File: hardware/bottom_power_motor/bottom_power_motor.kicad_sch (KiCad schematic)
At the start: 102 parts, among them J1 Power/Motor 6p, J2 J_STK_A, J3 J_STK_B, Q1 P-FET 40V 30A, U1 L78L12, U2 TPS54360, U2_CB 100n, U2_CO 47u, U2_CZ 3n3, U2_D 60V 3A, U2_L 10u, U2_RC 10k, U2_RH 53k6, U2_RL 10k2, U2_RT_R 100k, U3 TLV62569, U4 TPS54360, U4_CB 100n, U4_CO 22u, U4_CZ 3n3, U4_D 60V 3A, U4_L 33u, U4_RC 10k, U4_RH 68k1, U4_RL 10k0, U4_RT_R 100k

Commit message: Reed-Kontakte, Haubenkontakt, Klinkenbuchse, ToF statt Radar
Funktional neu
--------------
- Zwei Reed-Eingaenge fuer Fensterkontakte auf den einzigen noch freien
  Expanderpins P6/P7. 10k Pullup, 1k Serie, 100n und TVS je Kanal; bei
  geschlossenem Kontakt liegen 0,3 V am PCF8574, sicher unter VIL.
- Meldekontakt zur Dunstabzugshaube ueber PhotoMOS AQY282GS statt Relais:
  potentialfrei, 60 V / 0,8 A, kein Spulenstrom, keine Bauhoehe im 9-mm-
  Stapelspalt. NUR SELV - bei 230 V gehoert das Schaltglied nicht in die Dose.
- Weihnachtsstern jetzt gesteckt: Klinkenbuchse im oberen Steg der
  Frontplatte, PTC 0,2 A direkt an der Buchse gegen den Kurzschluss beim
  Stecken, Bulk vor die Sicherung gelegt.
- Radar durch VL53L1X (ToF) ersetzt. Hinter dieser Frontplatte hat kein
  20-mm-Radarmodul freie Sicht; der ToF passt als 4,9 x 2,5 mm grosser Chip
  in den Steg. Er misst Entfernung statt Empfindlichkeit - Schwelle exakt
  1 m - und deckt in der Fensterlaibung zugleich den Durchstieg ab.
  Netze umbenannt: RADAR_INT -> PRESENCE_INT, UART_RADAR_* -> UART_AUX_*.
  J7 bleibt unbestueckt als Reserve, damit das Stackpinout unberuehrt bleibt.

Frontplatte
-----------
Oberer Steg 9 -> 17 mm, damit Klinkenbuchse und ToF-Fenster nebeneinander
passen; Sicheln dadurch ~70 -> ~45 Grad, Stoesselwinkel 18 -> 12 Grad.
ToF-Kanal konisch (4,5 vorn, 3,0 hinten) fuer den Sichtkegel. Kabelausgang
Ø4,5 entfaellt. Selbsttests bestanden, STEP/STL neu erzeugt.

KiCad 10
--------
Die Generatoren liefen nur gegen KiCad-9-Bibliotheken. Migriert:
- Symbol- und Footprintpfad werden gefunden (Linux, macOS, Umgebungsvariable)
- PCF8574 -> PCF8574T (pinkompatibel, als Alias)
- Q_NMOS_GDS/Q_PMOS_GSD/Q_NPN_BCE liegen jetzt als hardware/lib/
  SwitchStack.kicad_sym im Projekt. KiCad 10 nummeriert die Stockvarianten
  mit G/D/S bzw. B/C/E - ein Alias haette die Anschluesse still vertauscht.
- USB-C-Schirm heisst SH statt S1, Zonen-API SetDoNotAllowZoneFills,
  DRC laeuft ueber kicad-cli statt WriteDRCRepo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
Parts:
- Q1: symbol Device:Q_PMOS_GSD -> SwitchStack:Q_PMOS_GSD
- Q_M1A_H, Q_M1A_L, Q_M1B_H, Q_M1B_L, Q_M2A_H, Q_M2A_L, Q_M2B_H, Q_M2B_L: symbol Device:Q_NMOS_GDS -> SwitchStack:Q_NMOS_GDS
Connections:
- net RADAR_INT renamed PRESENCE_INT
- net UART_RADAR_RX renamed UART_AUX_RX
- net UART_RADAR_TX renamed UART_AUX_TX
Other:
- moved on the sheet: R_M1_SH, R_M2_SH

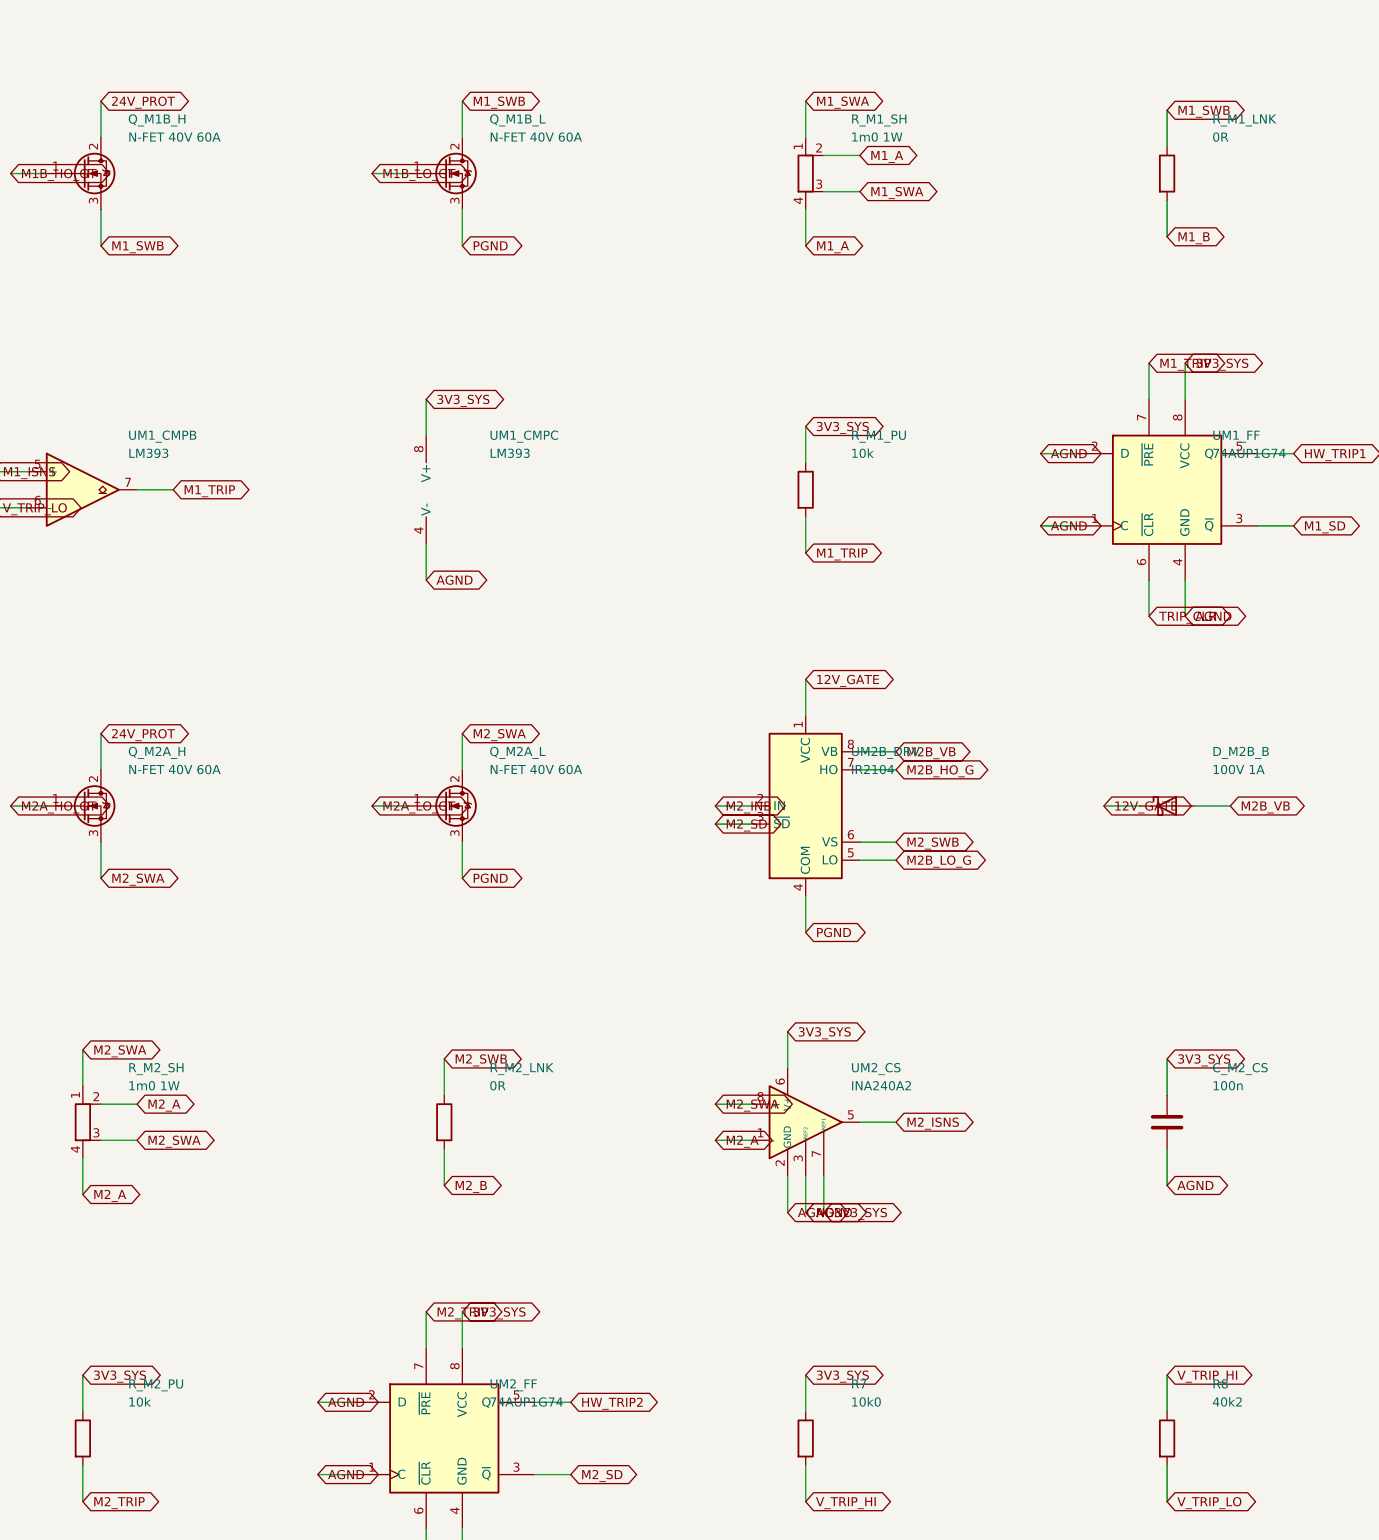
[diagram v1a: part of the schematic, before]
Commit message: Blockierstrom gemessen: 1,6 A statt 25 A - Auslegung neu gerechnet
Am 17.08.2026 mit blockiertem Abtrieb gemessen: 1,6 A bei 24 V, Netzteil mit
5 A Reserve, also keine Strombegrenzung. Daraus R_Anker = 15 Ohm. Die Messung
vom Vortag (0,116 A bei 2 V, 17,2 Ohm) bestaetigt das aus einem zwoelffach
anderen Betriebspunkt - die Zwischenbewertung "unbrauchbar" war falsch und ist
zurueckgenommen. Aufgeloest ist damit auch der Widerspruch zum Typenschild:
24 V an 15 Ohm ergeben maximal 38 W, die 100 W sind die Netzteilempfehlung der
Anlage, nicht die Aufnahme eines Motors.

GEAENDERTE WERTE - kein Layout betroffen:

  Shunt R_M1_SH/R_M2_SH   1 mOhm -> 5 mOhm    (gleicher Footprint)
  Trip-Teiler R8          40k2   -> 30k9      (+/-22 A -> +/-4,0 A)
  Sicherung F1            15 A   -> 6,3 A traege
  Firmware-Skalierung     20 A/V -> 4 A/V

Der Shunt wird groesser, nicht kleiner: Er bestimmt nicht die Belastbarkeit,
sondern die Aufloesung. Am 1-mOhm-Shunt lagen zwischen Fahrt und Anschlag nur
30-65 mV, in der Groessenordnung des ADC-Rauschens. Mit 5 mOhm sind es
150-325 mV bei 0,25 V/A und +/-6,6 A Messbereich; die Verlustleistung betraegt
bei 2 A ganze 20 mW.

Die Trip-Schwelle muss UEBER dem Blockierstrom liegen, weil der Anschlag ohne
Endschalter ein normaler Betriebszustand ist - der Laden faehrt bei jeder Fahrt
kurz dagegen. 4,0 A gibt Faktor 2,5 Reserve, ein echter Kurzschluss liegt
Groessenordnungen darueber.

FEHLER IN DER FIRMWARE MITGEFUNDEN: Der Nullpunkt des INA240 wurde nirgends
abgezogen. Der Sensor haette im Stillstand 6,6 A gemeldet statt 0 A. Jetzt
Betragsbildung um einen einstellbaren Nullpunkt (Vorgabe 1,65 V), damit auch
die Richtungsumkehr am Inline-Shunt kein Vorzeichen mehr erzeugt.

WAS DIE MESSUNG ERLEDIGT: Punkt 1 (Blockierstrom), Punkt 2 (Steckverbinder -
Micro-Fit 3.0 reicht, Mini-Fit Jr. nicht noetig) und die Verschaerfung von
Punkt 3. Der Summenstrom faellt von 9 A auf 3,9 A im unguenstigsten Fall.
Ein Anlaufstrom ueber dem Blockierstrom existier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
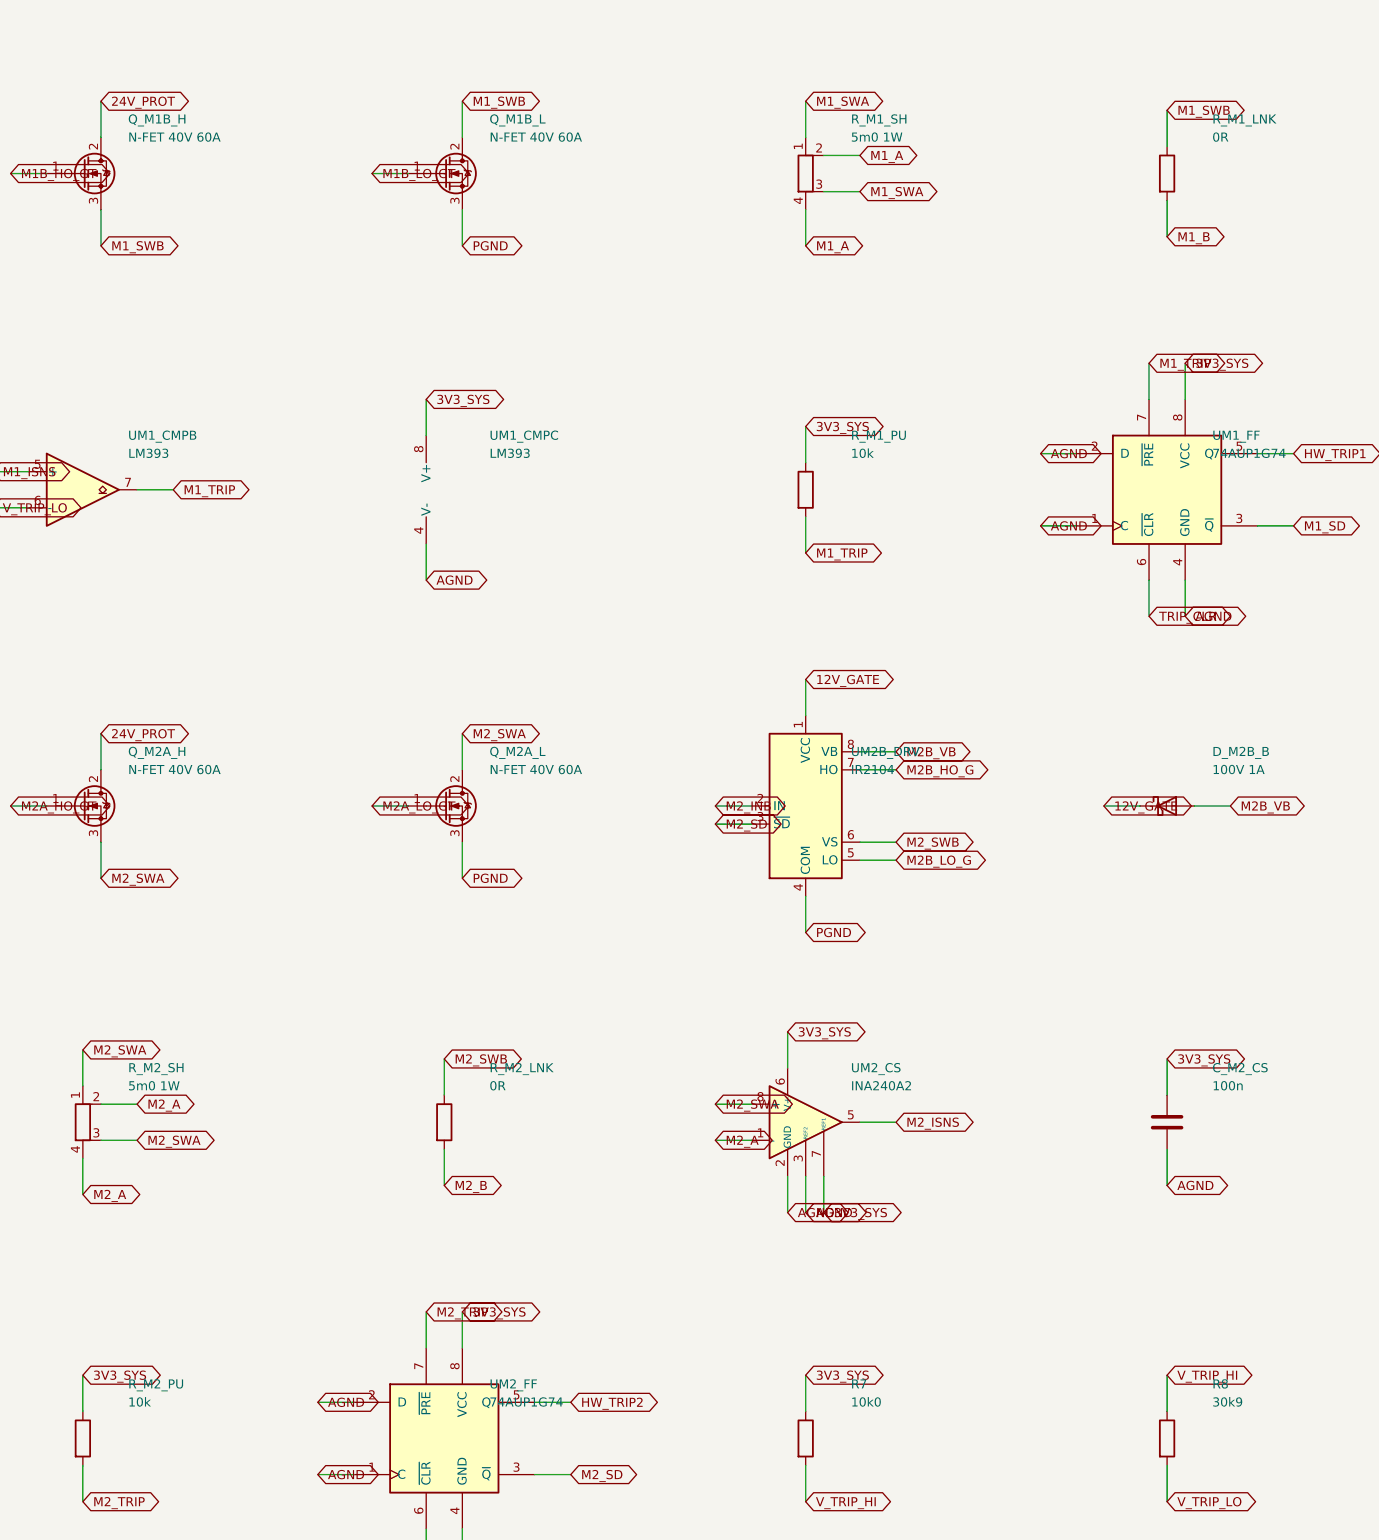
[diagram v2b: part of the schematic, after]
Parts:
- R7, R9: MPN Trip-Schwelle - messabhaengig -> Trip-Schwelle 4,0 A
- R8: value 40k2 -> 30k9; MPN Trip-Schwelle - messabhaengig -> Trip-Schwelle 4,0 A
- R_M1_SH, R_M2_SH: value 1m0 1W -> 5m0 1W
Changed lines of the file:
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@@
     (property "Reference" "R_M1_SH" (at 387.3500 284.4800 0)
       (effects (font (size 1.27 1.27)) (justify left)))
-    (property "Value" "1m0 1W" (at 387.3500 287.0200 0)
+    (property "Value" "5m0 1W" (at 387.3500 287.0200 0)
       (effects (font (size 1.27 1.27)) (justify left)))
     (property "Footprint" "Resistor_SMD:R_2512_6332Metric" (at 381.0000 292.1000 0)
@@
     (property "Reference" "R_M2_SH" (at 285.7500 417.8300 0)
       (effects (font (size 1.27 1.27)) (justify left)))
-    (property "Value" "1m0 1W" (at 285.7500 420.3700 0)
+    (property "Value" "5m0 1W" (at 285.7500 420.3700 0)
       (effects (font (size 1.27 1.27)) (justify left)))
     (property "Footprint" "Resistor_SMD:R_2512_6332Metric" (at 279.4000 425.4500 0)
@@
     (property "Footprint" "Resistor_SMD:R_0603_1608Metric" (at 381.0000 469.9000 0)
       (effects (font (size 1.27 1.27)) hide))
-    (property "MPN" "Trip-Schwelle - messabhaengig" (at 381.0000 472.4400 0)
+    (property "MPN" "Trip-Schwelle 4,0 A" (at 381.0000 472.4400 0)
       (effects (font (size 1.27 1.27)) hide))
     (pin "1")
@@
     (property "Reference" "R8" (at 438.1500 462.2800 0)
       (effects (font (size 1.27 1.27)) (justify left)))
-    (property "Value" "40k2" (at 438.1500 464.8200 0)
+    (property "Value" "30k9" (at 438.1500 464.8200 0)
       (effects (font (size 1.27 1.27)) (justify left)))
     (property "Footprint" "Resistor_SMD:R_0603_1608Metric" (at 431.8000 469.9000 0)
       (effects (font (size 1.27 1.27)) hide))
-    (property "MPN" "Trip-Schwelle - messabhaengig" (at 431.8000 472.4400 0)
+    (property "MPN" "Trip-Schwelle 4,0 A" (at 431.8000 472.4400 0)
       (effects (font (size 1.27 1.27)) hide))
     (pin "1")
@@
     (property "Footprint" "Resistor_SMD:R_0603_1608Metric" (at 25.4000 514.3500 0)
       (effects (font (size 1.27 1.27)) hide))
-    (property "MPN" "Trip-Schwelle - messabhaengig" (at 25.4000 516.8900 0)
-      (effects (font (size 1.27 1.27)) hide))
-    (pin "1")
+    (property "MPN" "Trip-Schwelle 4,0 A" (at 25.4000 516.8900 0)
+      (effects (font (size 1.27 1.27)) hide))
+    (pin "1")

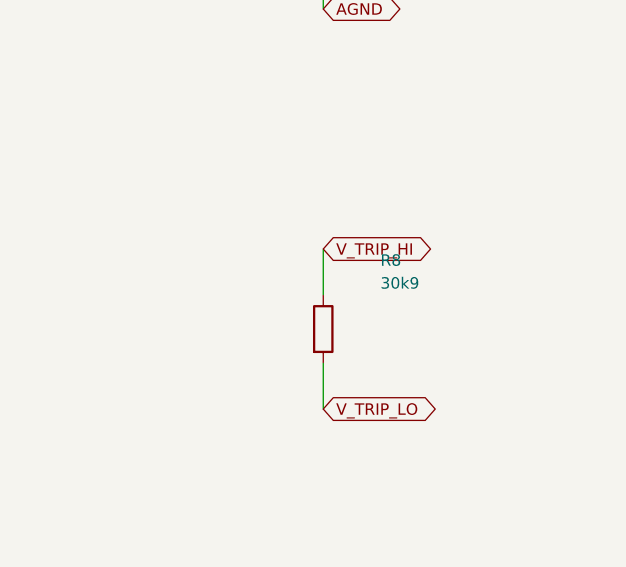
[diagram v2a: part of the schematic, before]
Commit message: Reserve nachgerechnet: Wind, Messfehler - und ein Fehler am Komparator
Nachgegangen der Frage, wie sicher der gemessene Blockierstrom ist und was bei
Wind passiert. Drei Ergebnisse, docs/11 Abschnitt 6 neu.

1) DER BLOCKIERSTROM IST EINE HARTE OBERGRENZE, keine Lastannahme. Bei
   blockiertem Laeufer ist die Gegenspannung null, also I = U/R. Ein Drehmoment
   kommt in der Gleichung nicht vor - Wind kann den Motor nur langsamer machen,
   und langsamer heisst naeher an 1,6 A, nie darueber. Ueberschritten wird die
   Grenze nur beim Umpolen eines noch drehenden Motors (bis 3,2 A), und dagegen
   stehen 300 ms Stoppause und die Selbsthemmung des Schneckengetriebes.

   Der Trip liegt mit 4,4 A ueber allen drei denkbaren Faellen.

2) TRIP-TEILER BLEIBT BEI 40k2 statt der gestern eingesetzten 30k9. Der
   groessere Shunt nimmt die Schwelle von allein von 22 A auf 4,4 A mit - ein
   Bauteil weniger geaendert, und die zusaetzliche Reserve kostet nichts, weil
   zwischen 4 und 5 A auf dieser Platine ohnehin nichts gefaehrdet ist. Damit
   traegt die Auslegung einen Messfehler von Faktor 2,5.

   Gegenprobe fuer Faktor 2 (3,2 A statt 1,6 A) in Abschnitt 6.2: Es reagieren
   genau zwei Positionen, und die Sicherung ist dabei kein Risiko, sondern der
   Melder - sie fliegt beim ersten beidseitigen Anschlag, harmlos und sofort
   sichtbar.

   Billige dritte Bestaetigung: M6 mit dem Multimeter ist bei 15 Ohm endlich
   brauchbar (Zuleitungen unter 3 % statt der Haelfte). Erwartet 14-17 Ohm,
   zwei Minuten, kein Blockieren.

3) WIND IST EIN MECHANISCHES PROBLEM. Ueberschlag fuer 0,84 m2 Flaeche: Ab
   etwa 40 km/h uebersteigt das Windmoment am Band die 25 Nm des Motors, bei
   90 km/h steht das Fuenffache dagegen. Elektrisch aendert das nichts, die
   Endlagenerkennung bricht aber in beide Richtungen: Gegenwind sieht aus wie
   ein Anschlag, Rueckenwind schlaegt den Fluegel bei NIEDRIGEREM Strom als
   normal gegen den Anschlag. Punkt 58 mit drei Gegenmassnahmen, davon die
   w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
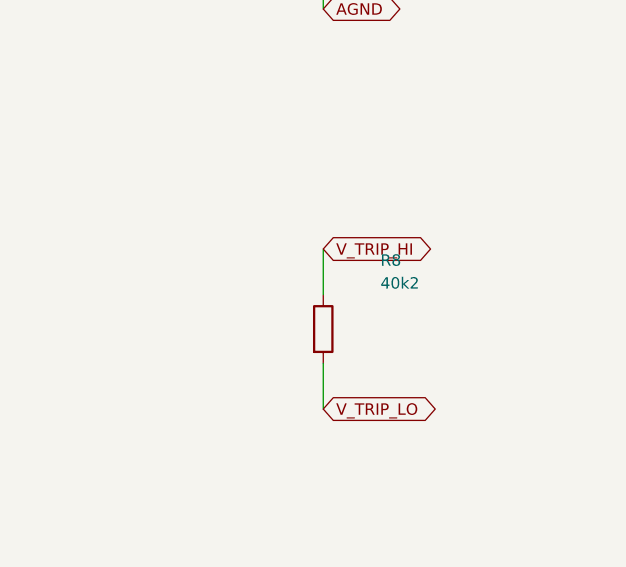
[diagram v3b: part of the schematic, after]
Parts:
- R7, R9: MPN Trip-Schwelle 4,0 A -> Trip-Schwelle 4,4 A
- R8: value 30k9 -> 40k2; MPN Trip-Schwelle 4,0 A -> Trip-Schwelle 4,4 A
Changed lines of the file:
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@@
     (property "Footprint" "Resistor_SMD:R_0603_1608Metric" (at 381.0000 469.9000 0)
       (effects (font (size 1.27 1.27)) hide))
-    (property "MPN" "Trip-Schwelle 4,0 A" (at 381.0000 472.4400 0)
+    (property "MPN" "Trip-Schwelle 4,4 A" (at 381.0000 472.4400 0)
       (effects (font (size 1.27 1.27)) hide))
     (pin "1")
@@
     (property "Reference" "R8" (at 438.1500 462.2800 0)
       (effects (font (size 1.27 1.27)) (justify left)))
-    (property "Value" "30k9" (at 438.1500 464.8200 0)
+    (property "Value" "40k2" (at 438.1500 464.8200 0)
       (effects (font (size 1.27 1.27)) (justify left)))
     (property "Footprint" "Resistor_SMD:R_0603_1608Metric" (at 431.8000 469.9000 0)
       (effects (font (size 1.27 1.27)) hide))
-    (property "MPN" "Trip-Schwelle 4,0 A" (at 431.8000 472.4400 0)
+    (property "MPN" "Trip-Schwelle 4,4 A" (at 431.8000 472.4400 0)
       (effects (font (size 1.27 1.27)) hide))
     (pin "1")
@@
     (property "Footprint" "Resistor_SMD:R_0603_1608Metric" (at 25.4000 514.3500 0)
       (effects (font (size 1.27 1.27)) hide))
-    (property "MPN" "Trip-Schwelle 4,0 A" (at 25.4000 516.8900 0)
+    (property "MPN" "Trip-Schwelle 4,4 A" (at 25.4000 516.8900 0)
       (effects (font (size 1.27 1.27)) hide))
     (pin "1")
